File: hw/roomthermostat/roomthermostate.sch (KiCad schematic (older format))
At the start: 58 parts, among them J1 ISP, J2 EXT TEMP SENSOR, J3 SPARE PINS, J4 EXT SWITCH 1 SIGNAL, J5 EXT SWITCH 1 GND, J6 EXT SWITCH 2 SIGNAL, J7 EXT SWITCH 2 GND, J8 TOUCHKEYS, J9 JTAG, Q1 BC846, U1 25LCXXX, U2 7,3728MHz, U3 TSIC306_TO92, U4 ATMEGA324-TQFP44, U5 EA-DOGM-132-XX

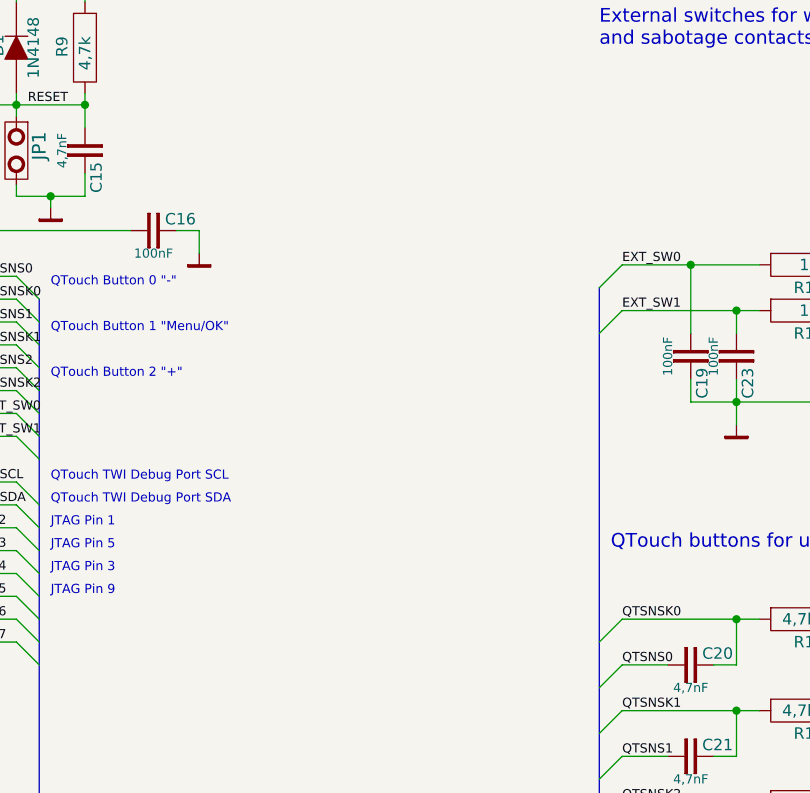
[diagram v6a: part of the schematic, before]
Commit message: Use bus-module_atmega328 instead of single atmega324 controller.
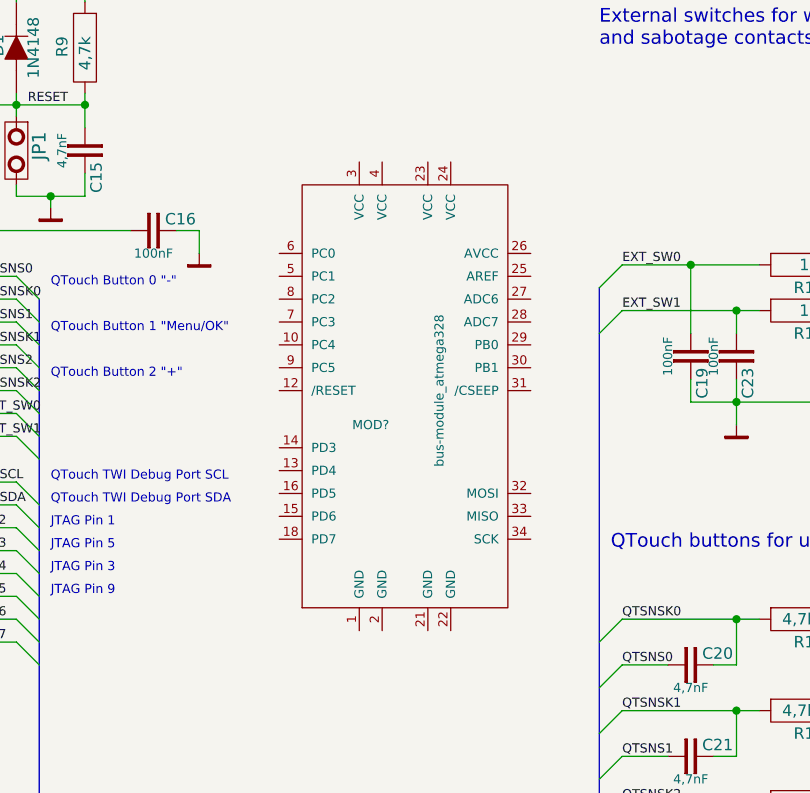
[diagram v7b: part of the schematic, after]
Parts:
- added MOD?: bus-module_atmega328, symbol bus-module_atmega328
